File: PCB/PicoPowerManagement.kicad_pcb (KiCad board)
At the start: 4 copper layers, 71.2 x 66 mm, 25 parts, among them J1 Conn_02x07_Odd_Even, J10 Conn_02x07_Odd_Even, J11 NAS Fan 1, J12 NAS Fan 2, J13 ATX 24P Connection, J15 Conn_01x02, J2 Conn_02x07_Odd_Even, J3 UART Header, J4 DEBUG, J5 SwitchLEDS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

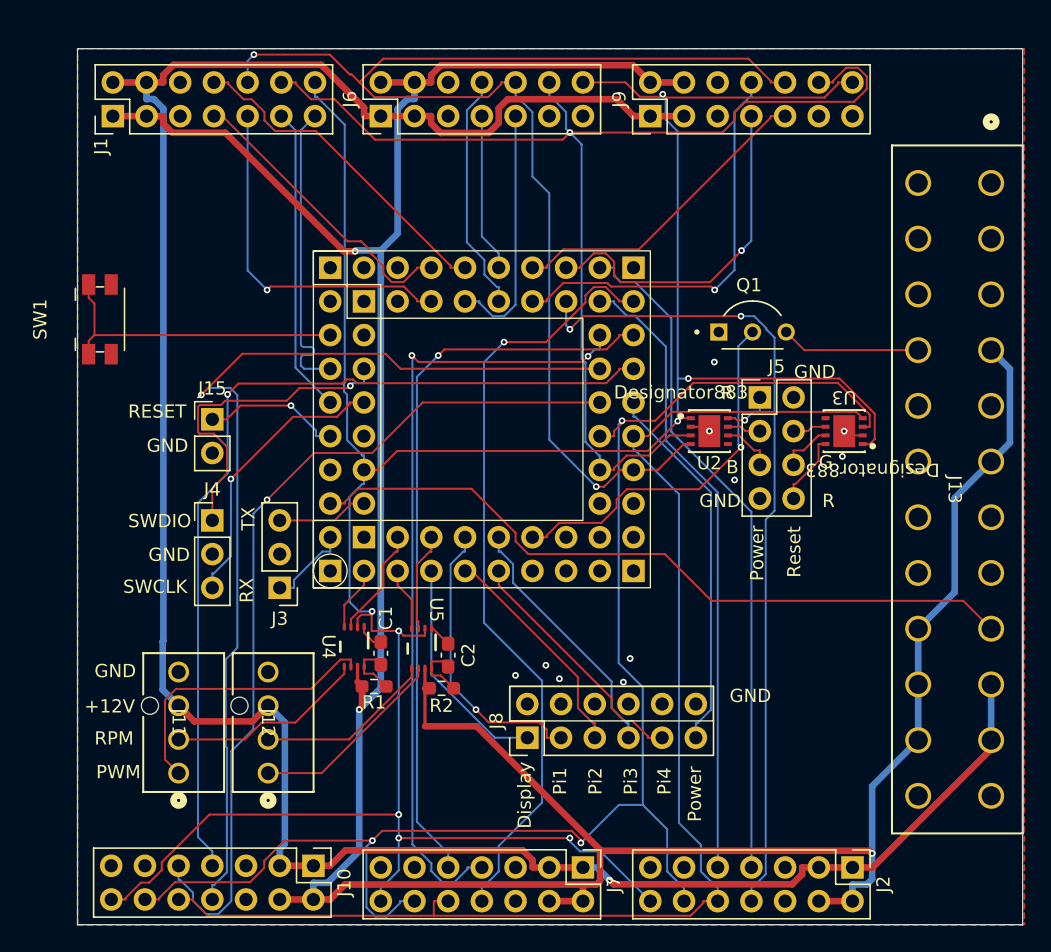
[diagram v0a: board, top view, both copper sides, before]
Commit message: Enhance PCB design and update UI for Raspberry Pi models
The most important changes in the `PicoPowerManagement.kicad_pcb` file focus on improving the PCB design's functionality and visual representation. Key updates include the removal of the option to plot invisible text and the addition of multiple mounting hole footprints with specific properties. Significant modifications were made to the layout, including adjustments to segments and paths to ensure compliance with updated specifications.

In the `PicoPowerManagement.kicad_pro` file, a new error check for "text_on_edge_cuts" was added to enhance the validation process. The `PicoPowerManagement.kicad_sch` files saw the addition of multiple mounting hole symbols with updated reference designators and footprints. Additionally, the `Home.razor` file was modified to display updated status information for Raspberry Pi models, changing labels from "Pi 3" and "Pi 4" to "PiDC" and "PiBuild," and adding shutdown buttons for each status display.
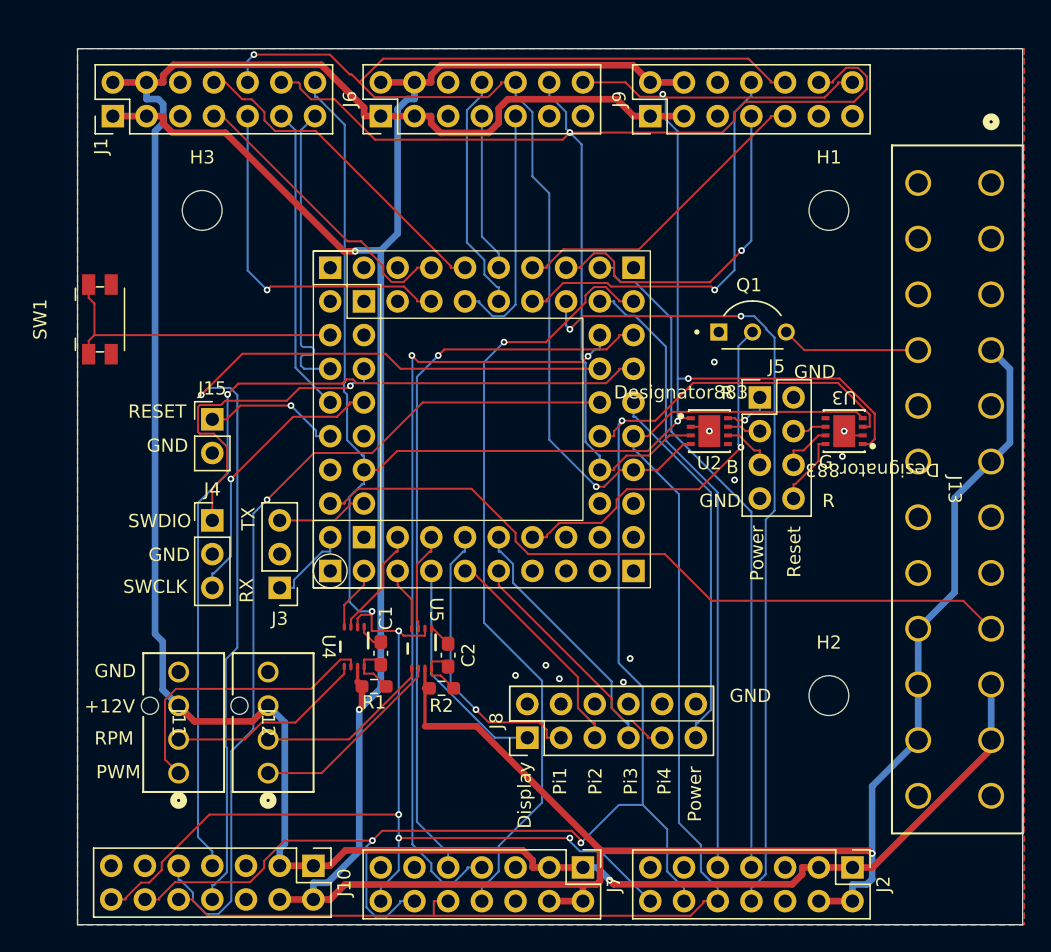
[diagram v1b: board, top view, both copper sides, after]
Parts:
- added H1: MountingHole, MountingHole:MountingHole_3mm, F.Cu at (82.0, 32.5)
- added H2: MountingHole, MountingHole:MountingHole_3mm, F.Cu at (82.0, 69.1)
- added H3: MountingHole, MountingHole:MountingHole_3mm, F.Cu at (34.8, 32.5)
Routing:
- net +12V: track 182.8 -> 183.5 mm

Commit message: simplifying USB
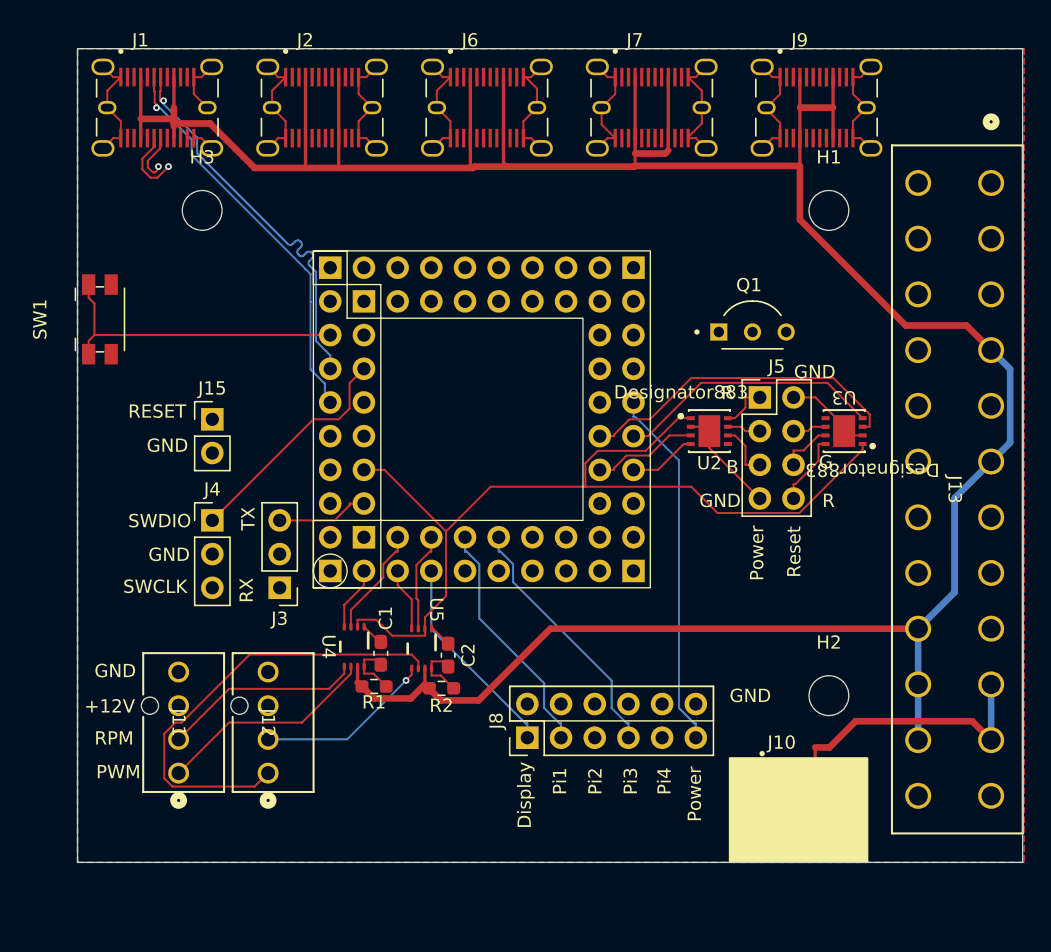
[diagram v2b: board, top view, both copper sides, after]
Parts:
- J1, J10, J2, J6, J7, J9: value Conn_02x07_Odd_Even -> 12401951E412A; footprint Connector_PinHeader_2.54mm:PinHeader_2x07_P2.54mm_Vertical -> USB-C:AMPHENOL_12401951E412A
- moved J2 69.9 mm to (43.8, 24.8), turned to 0 degrees
- moved J7 57.5 mm to (68.7, 24.8), turned to 0 degrees
- moved J10 36.8 mm to (79.8, 77.7), turned to 0 degrees
- moved J9 12.5 mm to (81.1, 24.8), turned to 0 degrees
- moved J6 8.03 mm to (56.3, 24.8), turned to 0 degrees
- moved J1 3.41 mm to (31.4, 24.8), turned to 0 degrees
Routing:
- net +3.3V: track 210.8 -> 69.9 mm, vias 8 -> 0
- net GND: track 6.78 -> 121.3 mm, vias 10 -> 0
- net SDA0: track 99.1 -> 5.13 mm, vias 2 -> 0
- net SCL1: track 114.7 -> 24.8 mm, vias 3 -> 0
- net SCL0: track 92.3 -> 8.01 mm, vias 1 -> 0
- net +12V: track 183.5 -> 99.2 mm, vias 1 -> 0
- net SDA1: track 100.0 -> 20.0 mm
- net /USB5_12VEN: track 73.9 -> 0.00 mm, vias 1 -> 0
- net /USB5_5VEN: track 68.6 -> 0.00 mm, vias 1 -> 0
- net /USB5_INT: track 66.4 -> 0.00 mm, vias 1 -> 0
- net /USB3_12VEN: track 62.1 -> 0.00 mm, vias 2 -> 0
- net /USB4_5VEN: track 60.0 -> 0.00 mm, vias 2 -> 0
- net /USB4_12VEN: track 58.8 -> 0.00 mm, vias 1 -> 0
- net /USB4_INT: track 55.7 -> 0.00 mm, vias 1 -> 0
- net /USB3_5VEN: track 51.2 -> 0.00 mm
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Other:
- board size 71.2 x 66 mm -> 71.2 x 61.3 mm
